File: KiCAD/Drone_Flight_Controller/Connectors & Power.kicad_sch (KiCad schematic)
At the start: 35 parts, among them J301 Conn_01x03_Pin, J302 Conn_01x04, J303 Conn_01x03_Pin, J304 XT60, J305 Conn_01x03_Pin, J306 Conn_01x03_Pin, Q301 BC556, Q302 BC546, Q303 BC556, Q304 BC546, Q305 BC556, Q306 BC546, Q307 BC556, Q308 BC546, U202 AS358, U203 AS358, U301 AS358, U302 AS358, U305 AS358

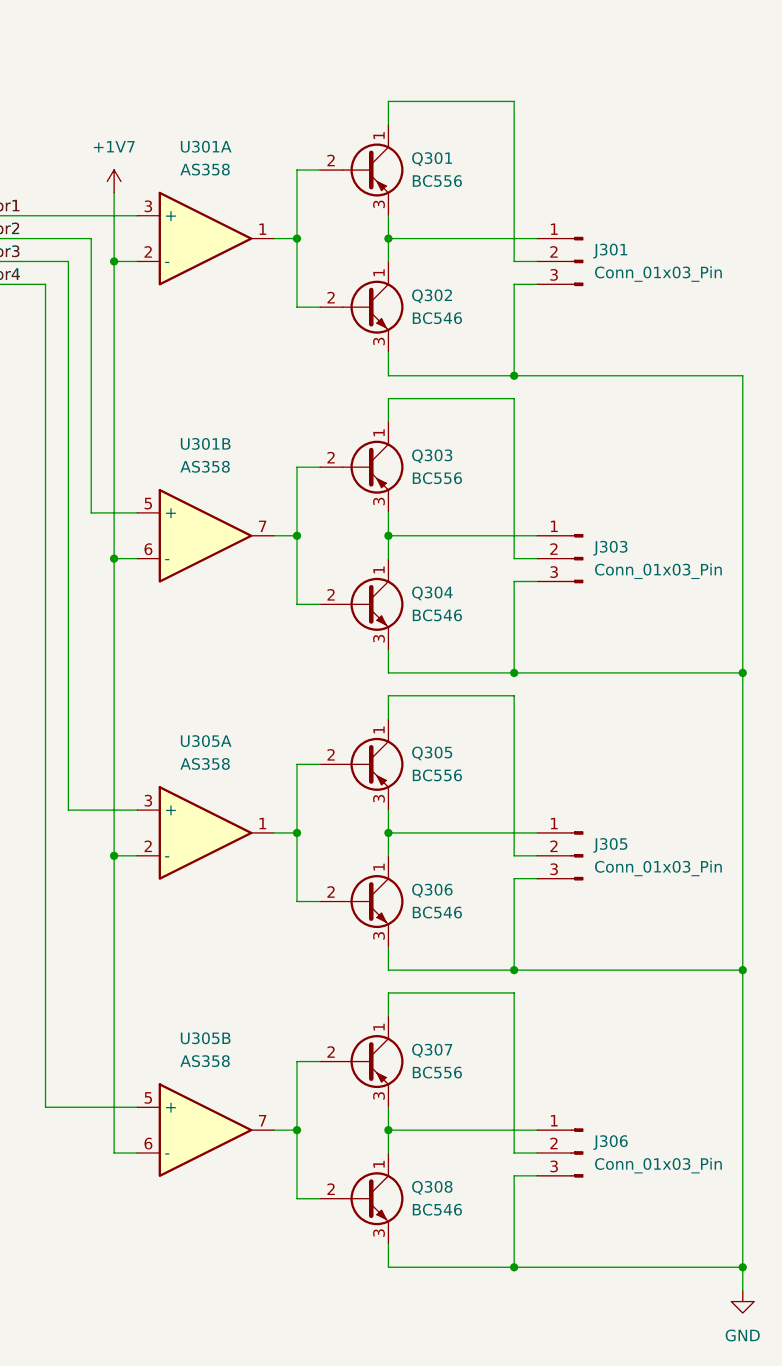
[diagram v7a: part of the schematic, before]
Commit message: Change Transistors to SMD Variants
Change Transistors to SMD Variants
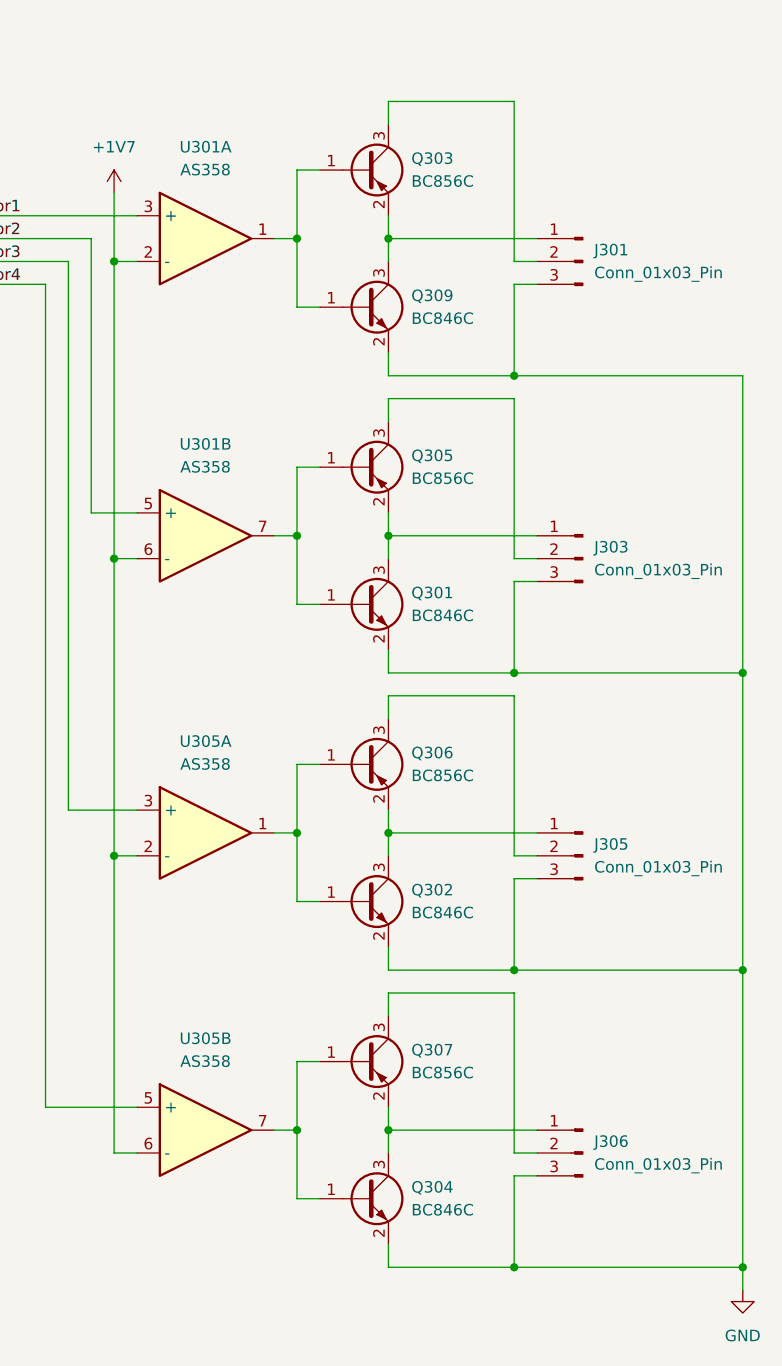
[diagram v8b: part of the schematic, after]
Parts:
- removed Q301, Q303, Q305, Q307: BC556, Package_TO_SOT_THT:TO-92_Inline, symbol Transistor_BJT:BC556
- removed Q302, Q304, Q306, Q308: BC546, Package_TO_SOT_THT:TO-92_Inline, symbol Transistor_BJT:BC546
- added Q301, Q302, Q304, Q309: BC846C, Package_TO_SOT_SMD:SOT-23, symbol Transistor_BJT:BC846
- added Q303, Q305, Q306, Q307: BC856C, Package_TO_SOT_SMD:SOT-23, symbol Transistor_BJT:BC856
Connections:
- net GND: now also Q301.2 (E), Q302.2 (E), Q304.2 (E), Q309.2 (E)
- net at J303.1 (Pin_1): now also Q301.3 (C), Q305.2 (E)
- net at U301.7: now also Q301.1 (B), Q305.1 (B)
- net at U305.1: now also Q302.1 (B), Q306.1 (B)
- net at U305.7: now also Q304.1 (B), Q307.1 (B)
- net at J301.1 (Pin_1): now also Q303.2 (E), Q309.3 (C)
- net at U301.1: now also Q303.1 (B), Q309.1 (B)
- net at J306.1 (Pin_1): now also Q304.3 (C), Q307.2 (E)
- net at J306.2 (Pin_2): now also Q307.3 (C)
- net at J303.2 (Pin_2): now also Q305.3 (C)
- net at J301.2 (Pin_2): now also Q303.3 (C)
- net at J305.2 (Pin_2): now also Q306.3 (C)
- net at J305.1 (Pin_1): now also Q302.3 (C), Q306.2 (E)
